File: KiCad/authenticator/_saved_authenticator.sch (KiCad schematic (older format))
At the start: 32 parts, among them J1 RPi_GPIO

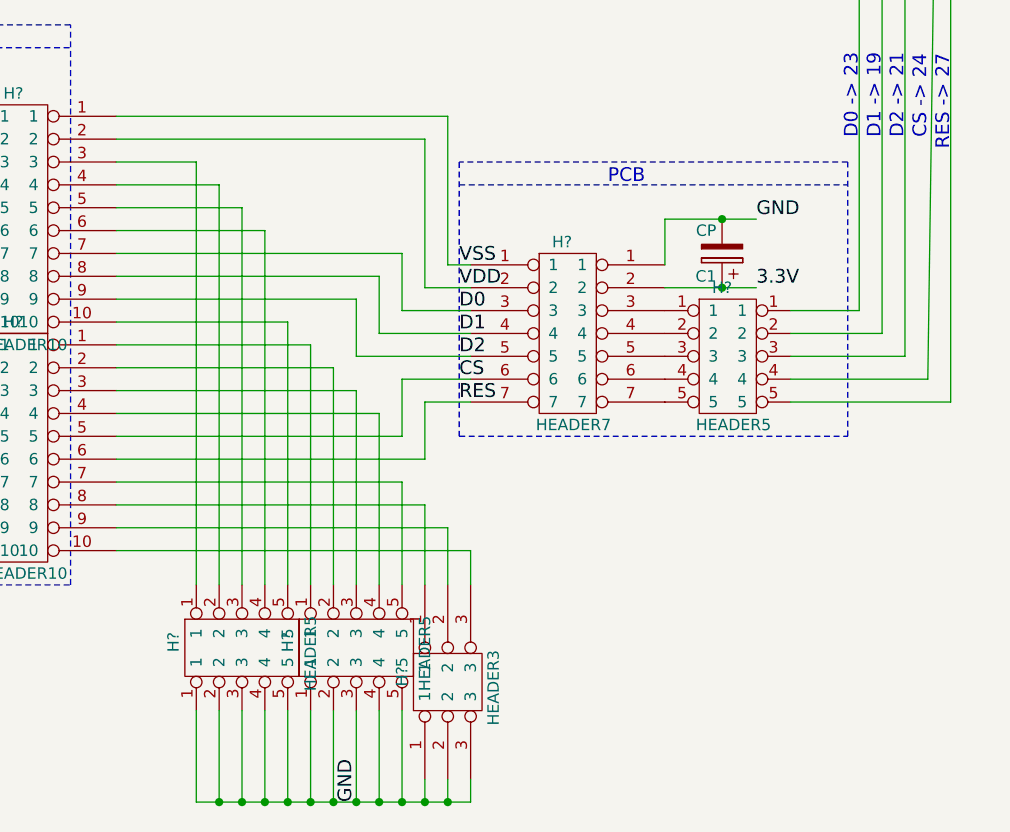
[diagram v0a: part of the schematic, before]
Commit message: Added cable headers to the schematics. Added cable headers to the component manifest.
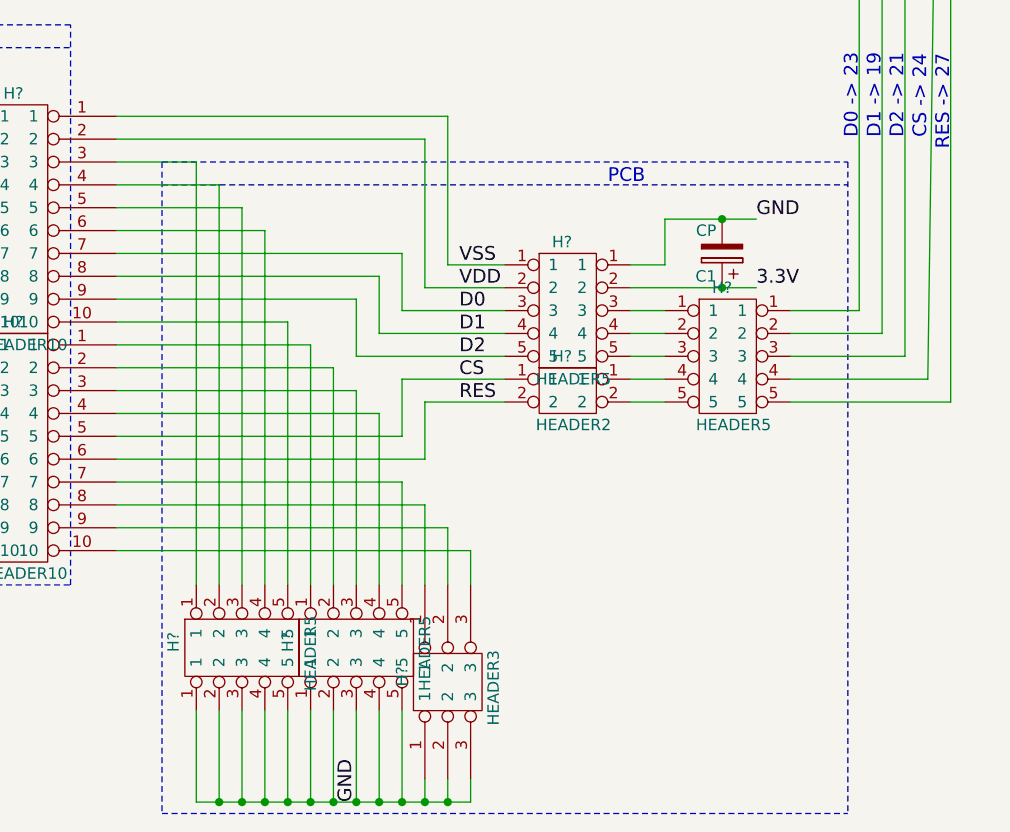
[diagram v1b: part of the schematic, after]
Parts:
- removed H?: HEADER7, symbol HEADER7
- added H?: HEADER2, symbol HEADER2
- added H?: HEADER5, symbol HEADER5
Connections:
- wire segments 181 -> 187
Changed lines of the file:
@@
 	0    -1   1    0
-$EndComp
-$Comp
-L HEADER7 H?
-U 1 1 57C6A281
-P 4800 5750
-F 0 "H?" H 4650 6250 50  0000 C CNN
-F 1 "HEADER7" H 4700 5450 50  0000 C CNN
-F 2 "" H 4800 5750 50  0000 C CNN
-F 3 "" H 4800 5750 50  0000 C CNN
-	1    4800 5750
-	1    0    0    -1
 $EndComp
 Text Label 4200 5350 0    60   ~ 0
@@
 	1300 1300 1300 1350
 Wire Notes Line
-	5900 4900 4200 4900
-Wire Notes Line
-	5900 6100 5900 4900
-Wire Notes Line
-	4200 6100 5900 6100
-Wire Notes Line
-	4200 4900 4200 6100
-Wire Notes Line
-	4200 5000 5900 5000
-Wire Wire Line
-	4050 5950 4250 5950
+	2900 4900 5900 4900
+Wire Notes Line
+	5900 4900 5900 7750
+Wire Notes Line
+	2900 4900 2900 7750
+Wire Notes Line
+	2900 5000 5900 5000
+Wire Wire Line
+	4050 5950 4400 5950
 Wire Wire Line
 	4050 6200 4050 5950
@@
 	2700 6200 4050 6200
 Wire Wire Line
-	3950 5850 4250 5850
+	3950 5850 4400 5850
 Wire Wire Line
 	3950 6100 3950 5850
@@
 	2700 6100 3950 6100
 Wire Wire Line
-	3750 5750 4250 5750
+	3750 5750 4400 5750
 Wire Wire Line
 	3750 5500 3750 5750
@@
 	2700 5500 3750 5500
 Wire Wire Line
-	3850 5650 4250 5650
+	3850 5650 4400 5650
 Wire Wire Line
 	3850 5400 3850 5650
@@
 	2700 5400 3850 5400
 Wire Wire Line
-	3950 5550 4250 5550
+	3950 5550 4400 5550
 Wire Wire Line
 	3950 5300 3950 5550
@@
 	2700 5300 3950 5300
 Wire Wire Line
-	4050 5450 4250 5450
+	4050 5450 4400 5450
 Wire Wire Line
 	4050 4800 4050 5450
@@
 	2700 4800 4050 4800
 Wire Wire Line
-	4150 5350 4250 5350
+	4150 5350 4400 5350
 Wire Wire Line
 	4150 4700 4150 5350
@@
 	5100 5150 5500 5150
 Wire Wire Line
-	5100 5450 5500 5450
+	4950 5450 5500 5450
 Wire Notes Line
 	9150 5050 11150 5050
@@
 Wire Wire Line
 	6950 2200 6350 2200
+Wire Notes Line
+	2900 7750 5900 7750
+$Comp
+L HEADER2 H?
+U 1 1 57CE05A5
+P 4800 6250
+F 0 "H?" H 4650 6750 50  0000 C CNN
+F 1 "HEADER2" H 4700 6450 50  0000 C CNN
+F 2 "" H 4800 6250 50  0000 C CNN
+F 3 "" H 4800 6250 50  0000 C CNN
+	1    4800 6250
+	1    0    0    -1
+$EndComp
+$Comp
+L HEADER5 H?
+U 1 1 57CE099C
+P 4800 5750
+F 0 "H?" H 4650 6250 50  0000 C CNN
+F 1 "HEADER5" H 4700 5650 50  0000 C CNN
+F 2 "" H 4800 5750 50  0000 C CNN
+F 3 "" H 4800 5750 50  0000 C CNN
+	1    4800 5750
+	1    0    0    -1
+$EndComp
+Wire Wire Line
+	4950 5350 5100 5350
+Wire Wire Line
+	4950 5550 5100 5550
+Wire Wire Line
+	5100 5650 4950 5650
+Wire Wire Line
+	4950 5750 5100 5750
+Wire Wire Line
+	5100 5850 4950 5850
+Wire Wire Line
+	4950 5950 5100 5950
 $EndSCHEMATC
